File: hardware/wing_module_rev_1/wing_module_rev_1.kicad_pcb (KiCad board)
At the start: 2 copper layers, 64 parts, among them J1 STRAIN, J2 TORSION, J3 Conn_01x03, J4 Conn_01x03, J5 Conn_01x04, J6 Conn_ST_STDC14, J7 Conn_01x04, J8 Conn_01x04, U1 ADS131M03IRUK, U2 STM32F103T8U6, U3 TCAN3403, U4 TPS563201, U5 TPS7A8101, U6 BL9161G-33

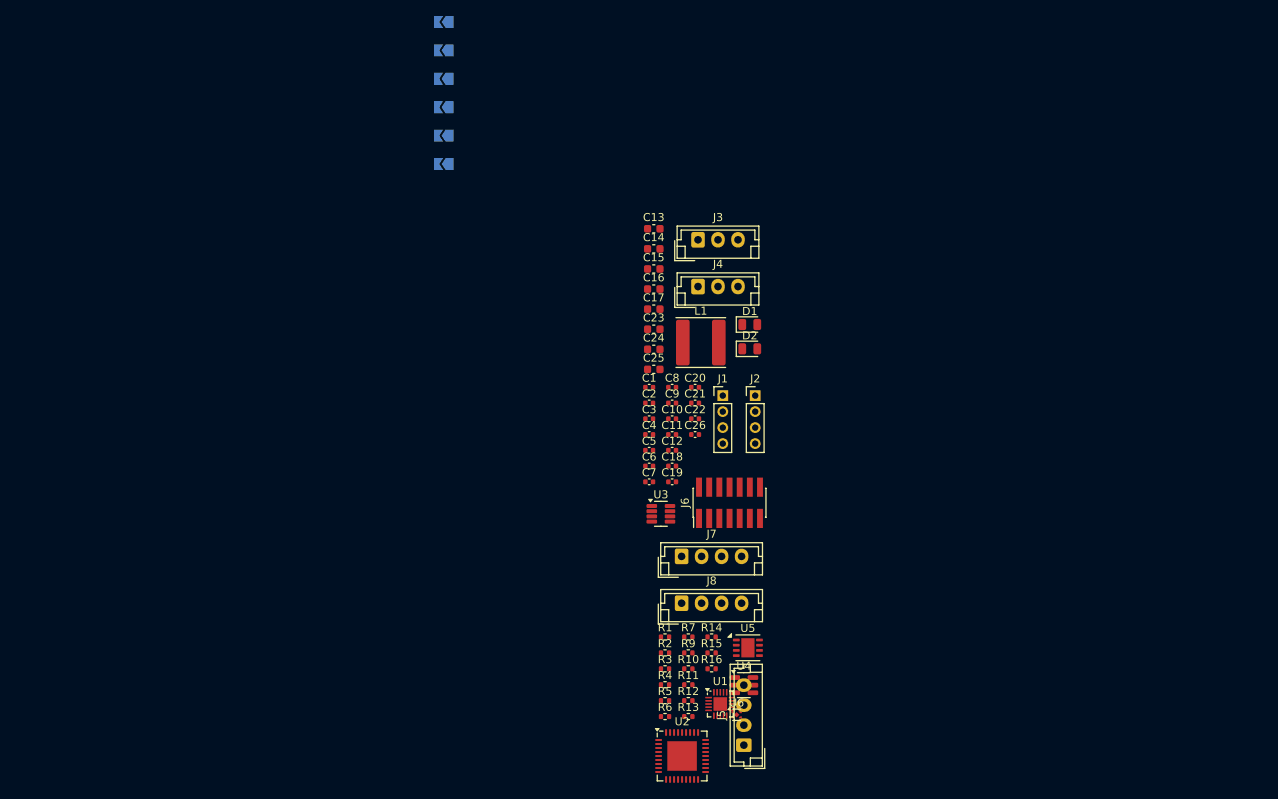
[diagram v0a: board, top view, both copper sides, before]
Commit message: Split up schematic into multple pages, added CS pullup for ADC
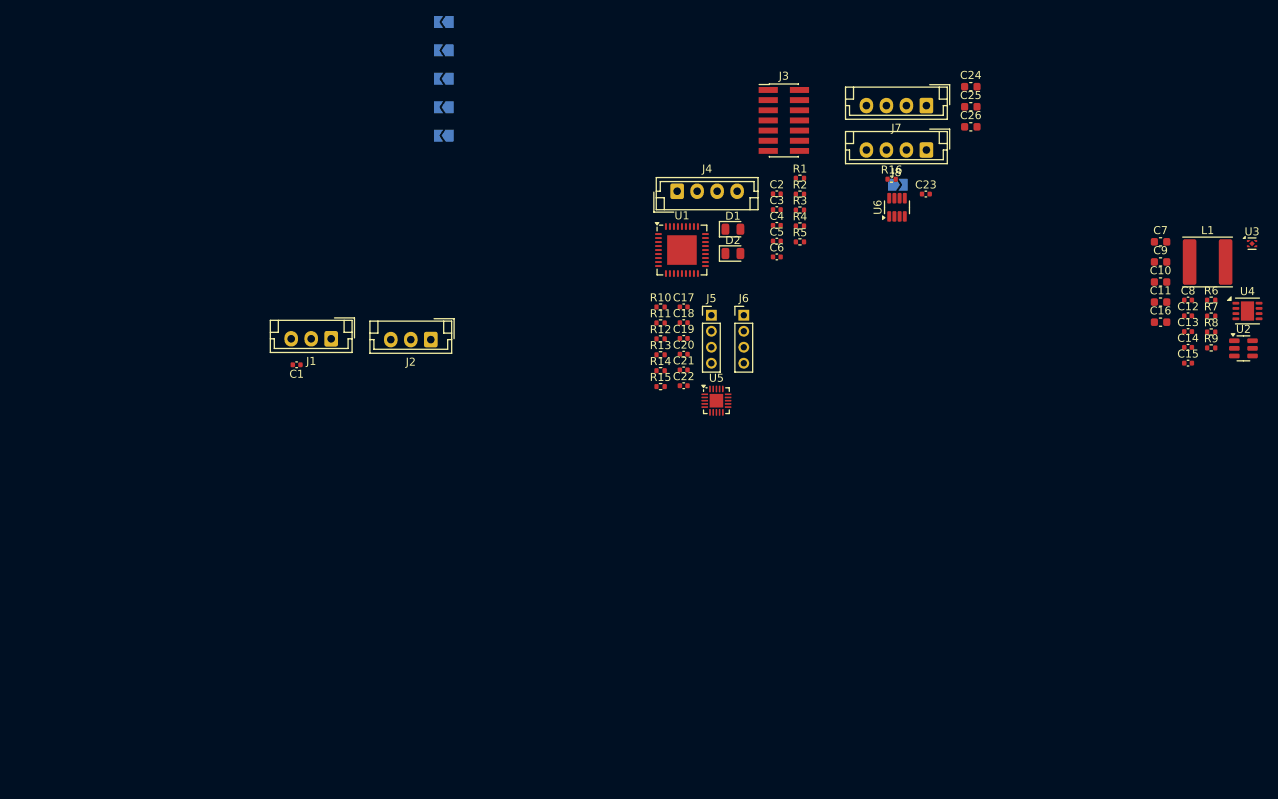
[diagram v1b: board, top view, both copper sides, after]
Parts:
- added R8: 30k9, Resistor_SMD:R_0402_1005Metric, F.Cu at (269.6, 79.1)
- C10, C9: value 100n -> 22u; footprint Capacitor_SMD:C_0402_1005Metric -> Capacitor_SMD:C_0603_1608Metric
- C11, C26: value 100n -> 10u; footprint Capacitor_SMD:C_0402_1005Metric -> Capacitor_SMD:C_0603_1608Metric
- C13, C15: value 10u -> 470n; footprint Capacitor_SMD:C_0603_1608Metric -> Capacitor_SMD:C_0402_1005Metric
- C14: value 10u -> 1u; footprint Capacitor_SMD:C_0603_1608Metric -> Capacitor_SMD:C_0402_1005Metric
- C17: value 10u -> 100n; footprint Capacitor_SMD:C_0603_1608Metric -> Capacitor_SMD:C_0402_1005Metric
- C18: value 470n -> 100n
- C19: value 470n -> 1u
- C20, C21, C4: value 1u -> 100n
- C22: value 100n -> 1u
- C23: value 22u -> 1u; footprint Capacitor_SMD:C_0603_1608Metric -> Capacitor_SMD:C_0402_1005Metric
- C24: value 22u -> 10u
- C7: value 1u -> 10u; footprint Capacitor_SMD:C_0402_1005Metric -> Capacitor_SMD:C_0603_1608Metric
- J1: value STRAIN -> Conn_01x03; footprint Connector_PinHeader_2.00mm:PinHeader_1x04_P2.00mm_Vertical -> Connector_JST:JST_EH_B3B-EH-A_1x03_P2.50mm_Vertical
- J2: value TORSION -> Conn_01x03; footprint Connector_PinHeader_2.00mm:PinHeader_1x04_P2.00mm_Vertical -> Connector_JST:JST_EH_B3B-EH-A_1x03_P2.50mm_Vertical
- J3: value Conn_01x03 -> Conn_ST_STDC14; footprint Connector_JST:JST_EH_B3B-EH-A_1x03_P2.50mm_Vertical -> Connector_PinHeader_1.27mm:PinHeader_2x07_P1.27mm_Vertical_SMD
- J4: value Conn_01x03 -> Conn_01x04; footprint Connector_JST:JST_EH_B3B-EH-A_1x03_P2.50mm_Vertical -> Connector_JST:JST_EH_B4B-EH-A_1x04_P2.50mm_Vertical
- J5: value Conn_01x04 -> STRAIN; footprint Connector_JST:JST_EH_B4B-EH-A_1x04_P2.50mm_Vertical -> Connector_PinHeader_2.00mm:PinHeader_1x04_P2.00mm_Vertical
- J6: value Conn_ST_STDC14 -> TORSION; footprint Connector_PinHeader_1.27mm:PinHeader_2x07_P1.27mm_Vertical_SMD -> Connector_PinHeader_2.00mm:PinHeader_1x04_P2.00mm_Vertical
- R1, R7, R9: value 120 -> 10k
- R10, R11, R12: value 10k -> 120
- R13: value 30k9 -> 10k 0.1%
- R14: value 10k -> 10k 0.1%
- R15: value 54k9 -> 10k
- R4, R5: value 10k 0.1% -> 10k
- R6: value 10k -> 54k9
- U1: value ADS131M03IRUK -> STM32F103T8U6; footprint Package_DFN_QFN:WQFN-20-1EP_3x3mm_P0.4mm_EP1.7x1.7mm -> Package_DFN_QFN:QFN-36-1EP_6x6mm_P0.5mm_EP3.7x3.7mm
- U2: value STM32F103T8U6 -> TPS563201; footprint Package_DFN_QFN:QFN-36-1EP_6x6mm_P0.5mm_EP3.7x3.7mm -> Package_TO_SOT_SMD:SOT-23-6
- U3: value TCAN3403 -> BL9161G-33; footprint Package_TO_SOT_SMD:TSOT-23-8 -> Package_DFN_QFN:UDFN-4-1EP_1x1mm_P0.65mm_EP0.48x0.48mm
- U4: value TPS563201 -> TPS7A8101; footprint Package_TO_SOT_SMD:SOT-23-6 -> Package_SON:VSON-8-1EP_3x3mm_P0.65mm_EP1.65x2.4mm
- U5: value TPS7A8101 -> ADS131M03IRUK; footprint Package_SON:VSON-8-1EP_3x3mm_P0.65mm_EP1.65x2.4mm -> Package_DFN_QFN:WQFN-20-1EP_3x3mm_P0.4mm_EP1.7x1.7mm
- U6: value BL9161G-33 -> TCAN3403; footprint Package_DFN_QFN:UDFN-4-1EP_1x1mm_P0.65mm_EP0.48x0.48mm -> Package_TO_SOT_SMD:TSOT-23-8
- moved U2 86.7 mm to (273.7, 81.1)
- moved R6 85.8 mm to (269.6, 75.1)
- moved U3 81.2 mm to (274.8, 68.1)
- moved U4 78.4 mm to (274.2, 76.5)
- moved R7 76.7 mm to (269.6, 77.1)
- moved R9 75.7 mm to (269.6, 81.1)
- moved C7 70.6 mm to (263.3, 67.8)
- moved C13 68.0 mm to (266.8, 79.0)
- moved C14 67.9 mm to (266.8, 81.0)
- moved C15 67.8 mm to (266.8, 83.0)
- moved C12 66.6 mm to (266.8, 77.1)
- moved U6 66.5 mm to (230.4, 63.5), turned to 90 degrees
- moved C8 65.4 mm to (266.8, 75.1)
- moved R16 65.2 mm to (229.7, 60.0)
- moved J8 64.4 mm to (234.1, 56.4), turned to 180 degrees
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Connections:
- C1 pad 1: /ADC_{B}+ -> /POT
- C1 pad 2: /ADC_{B}- -> GND
- C10 pad 1: +3V3 -> +5V
- C11 pad 1: +3.3VA -> +5V
- C12 pad 1: +3V3 -> +5V
- C13 pad 1: +BATT -> Net-(U4-NR)
- C14 pad 1: +BATT -> +3V3
- C15 pad 1: +BATT -> +3.3VA
- C15 pad 2: GND -> Net-(U4-FB)
- C16 pad 1: +5V -> +3.3VA
- C17 pad 1: +3.3VA -> /Strain Gauges/ADC_{B}+
- C17 pad 2: GND -> /Strain Gauges/ADC_{B}-
- C18 pad 1: Net-(U5-NR) -> /Strain Gauges/ADC_{A}-
- C18 pad 2: GND -> /Strain Gauges/ADC_{A}+
- C19 pad 2: Net-(U5-FB) -> GND
- C2 pad 1: /POT -> +3.3VA
- C20 pad 1: +5V -> Net-(U5-CAP)
- C21 pad 1: +3V3 -> Net-(U5-CAP)
- C22 pad 1: Net-(U4-VBST) -> +3V3
- C22 pad 2: Net-(U4-SW) -> GND
- C23 pad 1: +5V -> +3V3
- C24 pad 1: +5V -> +BATT
- C26 pad 1: Net-(U1-CAP) -> +BATT
- C3 pad 1: /ADC_{A}- -> +3V3
- C3 pad 2: /ADC_{A}+ -> GND
- C4 pad 1: +3.3VA -> +3V3
- C5 pad 1: Net-(U1-CAP) -> +3V3
- C7 pad 1: +3V3 -> +BATT
- C8 pad 1: +3V3 -> Net-(U2-VBST)
- C8 pad 2: GND -> Net-(U2-SW)
- C9 pad 1: +3V3 -> +5V
- J1 pad 1: GND -> +3.3VA
- J1 pad 2: /IN_{A}- -> /POT
- J1 pad 3: /IN_{A}- -> GND
- J2 pad 2: /IN_{B}- -> +5V
- J2 pad 3: /IN_{B}+ -> /SERVO
- J3 pad 1: GND -> unconnected-(J3-NC-Pad1)
- J3 pad 2: +5V -> unconnected-(J3-NC-Pad2)
- J3 pad 3: /SERVO -> +3V3
- J4 pad 1: +3.3VA -> GND
- J4 pad 2: /POT -> /SCL
- J4 pad 3: GND -> /SDA
- J5 pad 2: /SCL -> /Strain Gauges/IN_{A}-
- J5 pad 3: /SDA -> /Strain Gauges/IN_{A}-
- J5 pad 4: +5V -> +3.3VA
- J6 pad 1: unconnected-(J6-NC-Pad1) -> GND
- J6 pad 2: unconnected-(J6-NC-Pad2) -> /Strain Gauges/IN_{B}-
- J6 pad 3: +3V3 -> /Strain Gauges/IN_{B}+
- J6 pad 4: /SWDIO -> +3.3VA
- J7 pad 2: /CANL -> /CAN/CANL
- J7 pad 3: /CANH -> /CAN/CANH
- J8 pad 2: /CANL -> /CAN/CANL
- J8 pad 3: /CANH -> /CAN/CANH
- JP6 pad 2: /CANL -> /CAN/CANL
- L1 pad 1: Net-(U4-SW) -> Net-(U2-SW)
- R1 pad 1: /IN_{A}- -> +3V3
- R1 pad 2: /ADC_{A}- -> /~{RST}
- R10 pad 1: +3V3 -> /Strain Gauges/IN_{A}-
- R10 pad 2: /SDA -> /Strain Gauges/ADC_{A}-
- R11 pad 1: +3V3 -> /Strain Gauges/IN_{B}+
- R11 pad 2: /SCL -> /Strain Gauges/ADC_{B}+
- R12 pad 1: Net-(U5-FB) -> /Strain Gauges/IN_{B}-
- R12 pad 2: GND -> /Strain Gauges/ADC_{B}-
- R13 pad 2: Net-(U5-FB) -> /Strain Gauges/ADC_{A}+
- R14 pad 1: Net-(U4-VFB) -> /Strain Gauges/ADC_{A}+
- R15 pad 1: +5V -> +3V3
- R15 pad 2: Net-(U4-VFB) -> /Strain Gauges/~{CS}_{ADC}
- R16 pad 1: /LED_{WHITE} -> /CAN/CANH
- R16 pad 2: Net-(D2-A) -> Net-(JP6-A)
- R2 pad 1: /IN_{B}+ -> /LED_{RED}
- R2 pad 2: /ADC_{B}+ -> Net-(D1-A)
- R3 pad 1: /IN_{B}- -> /LED_{WHITE}
- R3 pad 2: /ADC_{B}- -> Net-(D2-A)
- R4 pad 1: +3.3VA -> +3V3
- R4 pad 2: /ADC_{A}+ -> /SDA
- R5 pad 1: /ADC_{A}+ -> +3V3
- R5 pad 2: GND -> /SCL
- R6 pad 1: +3V3 -> +5V
- R6 pad 2: /~{RST} -> Net-(U2-VFB)
- R7 pad 1: /LED_{RED} -> Net-(U2-VFB)
- R7 pad 2: Net-(D1-A) -> GND
- R9 pad 1: /CANH -> Net-(U4-FB)
- R9 pad 2: Net-(JP6-A) -> GND
- U1 pad 1: /ADC_{A}+ -> +3V3
- U1 pad 10: /~{CS}_{ADC} -> /~{DRDY}
- U1 pad 11: /~{DRDY} -> /~{CS}_{ADC}
- U1 pad 15: /CLKIN -> /POT
- U1 pad 16: Net-(U1-CAP) -> /ADDR_{4}
- U1 pad 17: GND -> /ADDR_{3}
- U1 pad 18: +3V3 -> GND
- U1 pad 19: +3.3VA -> +3V3
- U1 pad 2: /ADC_{A}- -> unconnected-(U1-PD0-Pad2)
- U1 pad 20: GND -> /CLKIN
- U1 pad 21: GND -> /VCP_TX
- U1 pad 3: /ADC_{B}- -> unconnected-(U1-PD1-Pad3)
- U1 pad 4: /ADC_{B}+ -> /~{RST}
- U1 pad 5: unconnected-(U1-AIN_{2+}-Pad5) -> GND
- U1 pad 6: unconnected-(U1-AIN_{2-}-Pad6) -> +3.3VA
- U1 pad 7: unconnected-(U1-NC-Pad7) -> /LED_{RED}
- U1 pad 8: unconnected-(U1-NC-Pad8) -> /LED_{WHITE}
- U2 pad 1: +3V3 -> GND
- U2 pad 2: unconnected-(U2-PD0-Pad2) -> Net-(U2-SW)
- U2 pad 3: unconnected-(U2-PD1-Pad3) -> +BATT
- U2 pad 4: /~{RST} -> Net-(U2-VFB)
- U2 pad 5: GND -> +BATT
- U2 pad 6: +3.3VA -> Net-(U2-VBST)
- U3 pad 1: /CAN_TX -> +3V3
- U3 pad 3: +3V3 -> +5V
- U3 pad 4: /CAN_RX -> +5V
- U3 pad 5: +3V3 -> GND
- U4 pad 1: GND -> +3.3VA
- U4 pad 2: Net-(U4-SW) -> +3.3VA
- U4 pad 3: +BATT -> Net-(U4-FB)
- U4 pad 4: Net-(U4-VFB) -> GND
- U4 pad 5: +BATT -> +5V
- U4 pad 6: Net-(U4-VBST) -> Net-(U4-NR)
- U5 pad 1: +3.3VA -> /Strain Gauges/ADC_{A}+
- U5 pad 2: +3.3VA -> /Strain Gauges/ADC_{A}-
- U5 pad 3: Net-(U5-FB) -> /Strain Gauges/ADC_{B}-
- U5 pad 4: GND -> /Strain Gauges/ADC_{B}+
- U5 pad 5: +5V -> unconnected-(U5-AIN_{2+}-Pad5)
- U5 pad 6: Net-(U5-NR) -> unconnected-(U5-AIN_{2-}-Pad6)
- U5 pad 7: +5V -> unconnected-(U5-NC-Pad7)
- U5 pad 8: +5V -> unconnected-(U5-NC-Pad8)
- U5 pad 9: GND -> /Strain Gauges/~{RST}_{ADC}
- U6 pad 1: +3V3 -> /CAN_TX
- U6 pad 3: +5V -> +3V3
- U6 pad 4: +5V -> /CAN_RX
- U6 pad 5: GND -> +3V3

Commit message: Adjusted CAN connector order, drafting floorplan
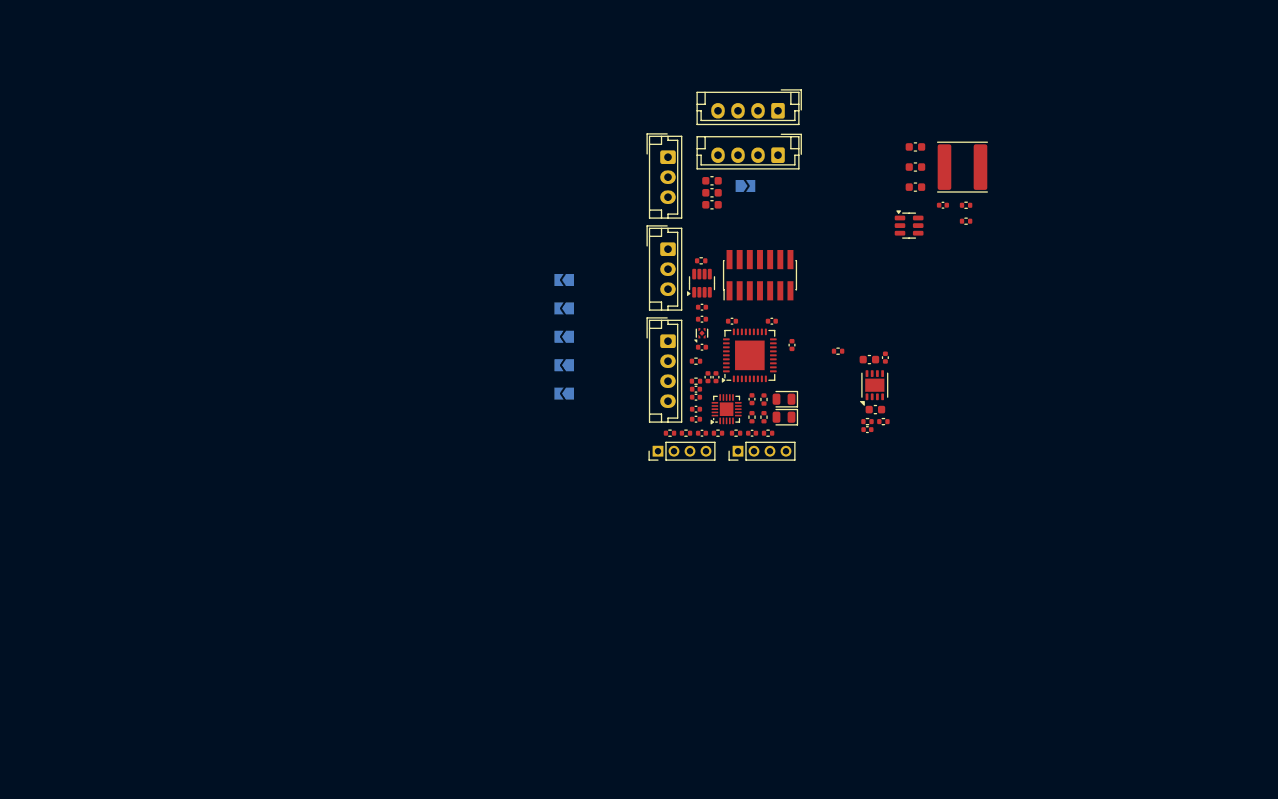
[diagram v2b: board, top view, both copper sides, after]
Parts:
- moved U3 69.7 mm to (206.0, 79.2), turned to 90 degrees
- moved C1 62.0 mm to (217.2, 80.7), turned to 90 degrees
- moved C12 60.8 mm to (206.0, 77.5)
- moved C14 60.8 mm to (206.0, 81.0)
- moved U4 47.5 mm to (227.6, 85.8), turned to 90 degrees
- moved U2 44.5 mm to (231.9, 65.8)
- moved R8 44.4 mm to (226.7, 90.3)
- moved J1 43.6 mm to (201.8, 68.8), turned to -90 degrees
- moved R9 42.0 mm to (228.7, 90.3)
- moved C15 40.9 mm to (226.7, 91.3)
- moved C13 38.0 mm to (228.9, 82.3), turned to 90 degrees
- moved J2 37.4 mm to (201.8, 57.2), turned to -90 degrees
- moved C16 37.3 mm to (227.7, 88.8)
- moved C11 37.1 mm to (226.9, 82.5)
- moved JP2 35.6 mm to (188.8, 76.2)
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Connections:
- J7 pad 2: /CAN/CANL -> +BATT
- J7 pad 3: /CAN/CANH -> /CAN/CANL
- J7 pad 4: +BATT -> /CAN/CANH
- J8 pad 2: /CAN/CANL -> +BATT
- J8 pad 3: /CAN/CANH -> /CAN/CANL
- J8 pad 4: +BATT -> /CAN/CANH
- R15 pad 2: /Strain Gauges/~{CS}_{ADC} -> /~{CS}_{ADC}
- U5 pad 10: /Strain Gauges/~{CS}_{ADC} -> /~{CS}_{ADC}
- U5 pad 11: /Strain Gauges/~{DRDY} -> /~{DRDY}
- U5 pad 12: /Strain Gauges/SCLK -> /SCLK
- U5 pad 13: /Strain Gauges/MISO -> /MISO
- U5 pad 14: /Strain Gauges/MOSI -> /MOSI
- U5 pad 15: /Strain Gauges/CLKIN -> /CLKIN
- U5 pad 9: /Strain Gauges/~{RST}_{ADC} -> /~{RST}_{ADC}

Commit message: Finished rev 1.0 layout of CAN
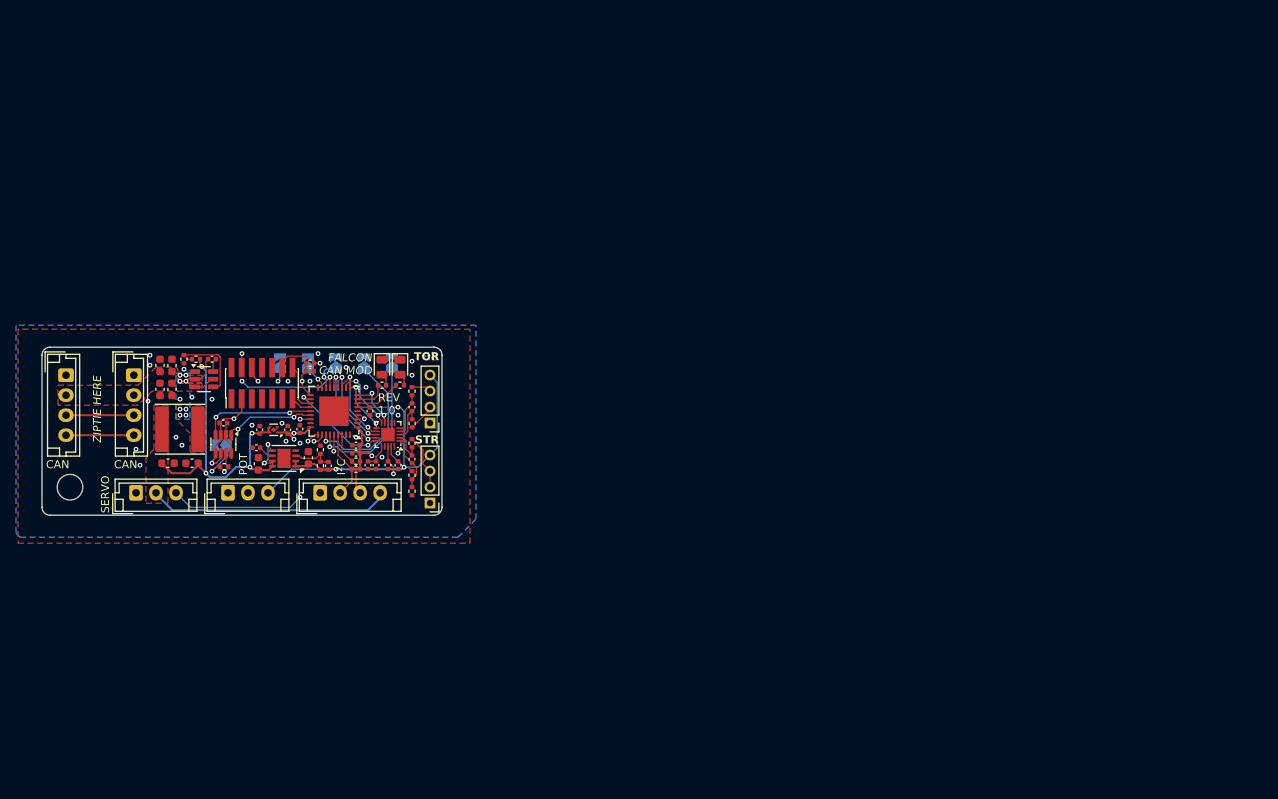
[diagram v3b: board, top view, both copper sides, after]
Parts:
- removed C1: 100n, Capacitor_SMD:C_0402_1005Metric
- removed R15: 10k, Resistor_SMD:R_0402_1005Metric
- added REF**: MountingHole_3.2mm_M3, MountingHole:MountingHole_3.2mm_M3, F.Cu at (127.0, 98.5)
- moved L1 103.2 mm to (140.8, 91.2), turned to 180 degrees
- moved C10 99.6 mm to (139.2, 95.5)
- moved R7 99.3 mm to (141.2, 82.5), turned to -90 degrees
- moved R6 98.2 mm to (142.8, 82.5), turned to 180 degrees
- moved C9 97.7 mm to (142.2, 95.5), turned to 180 degrees
- moved C7 96.9 mm to (139.8, 83.3), turned to 90 degrees
- moved J7 94.9 mm to (126.5, 84.5), turned to -90 degrees
- moved C8 93.4 mm to (144.8, 82.5), turned to 180 degrees
- moved U2 90.2 mm to (143.8, 85.0)
- moved J8 85.1 mm to (135.0, 84.5), turned to -90 degrees
- moved C13 79.4 mm to (150.3, 93.6), turned to 180 degrees
- moved J2 78.6 mm to (135.2, 99.2), turned to 0 degrees
- moved C11 77.5 mm to (150.6, 95.6), turned to 90 degrees
- moved U4 74.4 mm to (153.8, 94.9), turned to 180 degrees
- moved C25 73.2 mm to (138.2, 86.3), turned to -90 degrees
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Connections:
- J1 pad 1: +3.3VA -> GND
- J1 pad 3: GND -> +3.3VA
- U1 pad 16: /ADDR_{4} -> /ADDR_{2}
- U1 pad 17: /ADDR_{3} -> /ADDR_{1}
- U1 pad 30: /ADDR_{1} -> /ADDR_{3}
- U1 pad 31: /ADDR_{2} -> /ADDR_{4}
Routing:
- net +5V: track 0.00 -> 74.2 mm, vias 0 -> 6
- net +3.3VA: track 0.00 -> 56.6 mm, vias 0 -> 3
- net +3V3: track 0.00 -> 30.3 mm, vias 0 -> 6
- net /POT: track 0.00 -> 27.4 mm, vias 0 -> 2
- net /SERVO: track 0.00 -> 26.4 mm, vias 0 -> 2
- net /CAN/CANL: track 0.00 -> 25.2 mm, vias 0 -> 1
- net /CAN/CANH: track 0.00 -> 24.9 mm, vias 0 -> 1
- net /~{RST}: track 0.00 -> 20.0 mm, vias 0 -> 2
- net /ADDR_{3}: track 0.00 -> 19.0 mm, vias 0 -> 1
- net /ADDR_{4}: track 0.00 -> 18.4 mm, vias 0 -> 1
- net /CAN_RX: track 0.00 -> 14.5 mm, vias 0 -> 2
- net /SWDIO: track 0.00 -> 14.3 mm, vias 0 -> 2
- net /SWCLK: track 0.00 -> 13.7 mm, vias 0 -> 2
- net /CLKIN: track 0.00 -> 12.7 mm, vias 0 -> 2
- net /ADDR_{0}: track 0.00 -> 12.5 mm, vias 0 -> 2
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- added copper zone on B.Cu, net +3V3
- added copper zone on F.Cu, net +5V
- added copper zone on F.Cu, net +BATT
- added copper zone on F.Cu, net GND
- added copper zone on In1.Cu, net GND
- added copper zone on In2.Cu, net GND
- added copper zone on B.Cu, net Net-(U2-SW)
- added copper zone on F.Cu, net Net-(U2-SW)
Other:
- board outline added: 50 x 21 mm
- copper layers 2 -> 4
- board text added: "0"
- board text added: "0 mm"
- board text added: "0.0000 mm / 0.0000 mm"
- board text added: "0.01 mm"
- board text added: "0.02"
- board text added: "0.035 mm"
- board text added: "0.1 mm"
- board text added: "0.3000 mm"
- board text added: "1"
- board text added: "1.24 mm"
- board text added: "1.6000 mm"
- board text added: "16"
- board text added: "2"
- board text added: "3 S S G"
- board text added: "3 T T G"
- board text added: "3.3"
- board text added: "4"
- board text added: "4.5"
- board text added: "50.0000 mm x 21.0000 mm"
- board text added: "8"
- board text added: "B.Cu"
- board text added: "B.Mask"
- board text added: "B.Paste"
- board text added: "B.Silkscreen"
- board text added: "BOARD CHARACTERISTICS"
- board text added: "Board Thickness:"
- board text added: "Board overall dimensions:"
- board text added: "Bottom Silk Screen"
- board text added: "Bottom Solder Mask"
- board text added: "Bottom Solder Paste"
- board text added: "CAN"
- board text added: "CAN TERMINATION"
- board text added: "Castellated pads:"
- board text added: "Color"
- board text added: "Copper Finish:"
- board text added: "Copper Layer Count:"
- board text added: "Dielectric 1"
- board text added: "Dielectric 2"
- board text added: "Dielectric 3"
- board text added: "Edge card connectors:"
- board text added: "Epsilon R"
- board text added: "F.Cu"
- board text added: "F.Mask"
- board text added: "F.Paste"
- board text added: "F.Silkscreen"
- board text added: "FALCON CAN MOD"
- board text added: "FALCON CAN MODULE REV. ${REVISION}"
- board text added: "FR4"
- board text added: "FR4 natural"
- board text added: "G 5 P"
- board text added: "G S 3"
- board text added: "GND 12V CANL CANH"
- board text added: "GND SCL SDA 5V"
- board text added: "Green"
- board text added: "HAL SnPb"
- board text added: "I^{2}C"
- board text added: "Impedance Control:"
- board text added: "In1.Cu"
- board text added: "In2.Cu"
- board text added: "Layer Name"
- board text added: "Loss Tangent"
- board text added: "Material"
- board text added: "Min hole diameter:"
- board text added: "Min track/spacing:"
- board text added: "NODE ID"
- board text added: "No"
- board text added: "Not specified"
- board text added: "POT"
- board text added: "Plated Board Edge:"
- board text added: "REV ${REVISION}"
- board text added: "SB"
- board text added: "SERVO"
- board text added: "STR"
- board text added: "STRAIN"
- board text added: "TOR"
- board text added: "TORS"
- board text added: "Thickness (mm)"
- board text added: "Top Silk Screen"
- board text added: "Top Solder Mask"
- board text added: "Top Solder Paste"
- board text added: "Type"
- board text added: "White"
- board text added: "ZIPTIE HERE"
- board text added: "copper"
- board text added: "core"
- board text added: "prepreg"

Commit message: Reassigned reference numbers
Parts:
- renumbered C2 to C1, C11 to C10, C12 to C11, C13 to C12, C14 to C13, C15 to C14, C16 to C15, C17 to C16, C18 to C17, C19 to C18, C20 to C19, C3 to C2, C21 to C20, C22 to C21, C23 to C22, C24 to C23, C25 to C24, C26 to C25, C4 to C3, C5 to C4, C6 to C5, C7 to C6, C8 to C7, C9 to C8, C10 to C9, J8 to J7, J7 to J8, R16 to R15
